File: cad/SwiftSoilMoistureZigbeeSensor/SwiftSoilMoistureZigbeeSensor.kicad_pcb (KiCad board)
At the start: 2 copper layers, 12 parts, among them J1 Probe, J2 BAT, J3 TagConnect, Q1 BSS84, SW1 Factory Reset, U1 TPS61221DCK, U2 E73-2G4M08S1C

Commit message: CAD Stuff
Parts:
- added JP1: Jumper_Prog, Connector_PinHeader_2.54mm:PinHeader_1x02_P2.54mm_Vertical, F.Cu at (119.9, 71.2)
- J3: value TagConnect -> Conn_ARM_JTAG_SWD_10; footprint Connector:Tag-Connect_TC2030-IDC-NL_2x03_P1.27mm_Vertical -> Connector_PinHeader_1.27mm:PinHeader_2x05_P1.27mm_Vertical_SMD
- moved D1 64.9 mm to (112.0, 72.5)
- moved R1 64.6 mm to (107.5, 72.5)
- moved Q1 62.3 mm to (66.9, 68.7)
- moved SW1 62.3 mm to (99.4, 71.5)
- moved U2 62.3 mm to (82.2, 66.0)
- moved J1 61.1 mm to (61.5, 71.2)
- moved J3 60.9 mm to (109.1, 62.3), turned to 180 degrees
- moved C2 56.6 mm to (124.2, 60.3)
- moved U1 56.6 mm to (127.9, 60.5)
- moved C1 56.6 mm to (131.1, 60.3)
- moved L1 56.6 mm to (129.9, 65.4)
- moved J2 53.5 mm to (140.2, 63.6), turned to 180 degrees
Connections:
- C2 pad 1: +3.3V -> Net-(JP1-A)
- J3 pad 3: Net-(J3-~{RESET}) -> GND
- Q1 pad 2: +3.3V -> Net-(JP1-A)
- U1 pad 2: +3.3V -> Net-(JP1-A)
- U1 pad 4: +3.3V -> Net-(JP1-A)
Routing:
- net GND: track 0.00 -> 125.6 mm, vias 0 -> 1
- net Net-(JP1-A): track 0.00 -> 77.7 mm
- net Net-(J3-~{RESET}): track 0.00 -> 36.7 mm
- net +3.3V: track 38.2 -> 53.1 mm
- net Net-(J2-Pin_1): track 65.3 -> 74.7 mm
- net Net-(U2B-P0.24): track 8.08 -> 16.0 mm
- net Net-(J1-Pin_1): track 18.4 -> 15.3 mm
- net Net-(U2B-P0.13): track 23.2 -> 20.8 mm
- net Net-(J1-Pin_2): track 7.62 -> 6.35 mm
- net Net-(J3-SWCLK/TCK): track 19.5 -> 18.6 mm
- net Net-(J3-SWDIO/TMS): track 17.9 -> 18.6 mm
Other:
- board outline added: 83.8 x 22.9 mm

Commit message: Prints
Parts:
- J3: value Conn_ARM_JTAG_SWD_10 -> ARM SWD 10
- JP1: value Jumper_Prog -> Prog
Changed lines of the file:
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@@
     (property "ki_keywords" "Cortex Debug Connector ARM SWD JTAG")
     (attr smd)
-    (fp_text reference "J3" (at 0 -4.235) (layer "F.SilkS")
-        (effects (font (size 1 1) (thickness 0.15)))
-    )
-    (fp_text value "Conn_ARM_JTAG_SWD_10" (at 0 4.235) (layer "F.Fab")
+    (fp_text reference "J3" (at 1.1915 -4.9635) (layer "F.SilkS")
+        (effects (font (size 1 1) (thickness 0.15)))
+    )
+    (fp_text value "ARM SWD 10" (at 0 4.235) (layer "F.Fab")
         (effects (font (size 1 1) (thickness 0.15)))
     )
@@
     (property "ki_keywords" "LED diode")
     (attr smd)
-    (fp_text reference "D1" (at 0 -1.05) (layer "F.SilkS")
-        (effects (font (size 1 1) (thickness 0.15)))
-    )
-    (fp_text value "LED" (at 0 1.05) (layer "F.Fab")
+    (fp_text reference "D1" (at -1.0785 -1.05 90) (layer "F.SilkS")
+        (effects (font (size 1 1) (thickness 0.15)))
+    )
+    (fp_text value "LED" (at -1.0785 2.6565 90) (layer "F.Fab")
         (effects (font (size 1 1) (thickness 0.15)))
     )
@@
         (effects (font (size 1 1) (thickness 0.15)))
     )
-    (fp_text value "Jumper_Prog" (at 0 4.87) (layer "F.Fab")
+    (fp_text value "Prog" (at 0 4.87) (layer "F.Fab")
         (effects (font (size 1 1) (thickness 0.15)))
     )
@@
         (effects (font (size 1 1) (thickness 0.15)))
     )
-    (fp_text value "Factory Reset" (at 0 4.5) (layer "F.Fab")
+    (fp_text value "Factory Reset" (at 0 4.6735) (layer "F.Fab")
         (effects (font (size 1 1) (thickness 0.15)))
     )
@@
     (property "ki_keywords" "R res resistor")
     (attr smd)
-    (fp_text reference "R1" (at 0 -1.05) (layer "F.SilkS")
-        (effects (font (size 1 1) (thickness 0.15)))
-    )
-    (fp_text value "220ohms" (at 0 1.05) (layer "F.Fab")
+    (fp_text reference "R1" (at 0 2.4235 90) (layer "F.SilkS")
+        (effects (font (size 1 1) (thickness 0.15)))
+    )
+    (fp_text value "220ohms" (at 1.7085 -0.1165 90) (layer "F.Fab")
         (effects (font (size 1 1) (thickness 0.15)))
     )
@@
         (effects (font (size 1 1) (thickness 0.15)))
     )
-    (fp_text value "E73-2G4M08S1C" (at 1.905 10.795) (layer "F.Fab")
-        (effects (font (size 1 1) (thickness 0.15)))
-    )
+    (fp_text value "E73-2G4M08S1C" (at 1.631 11.48) (layer "F.Fab")
+        (effects (font (size 1 1) (thickness 0.15)))
+    )

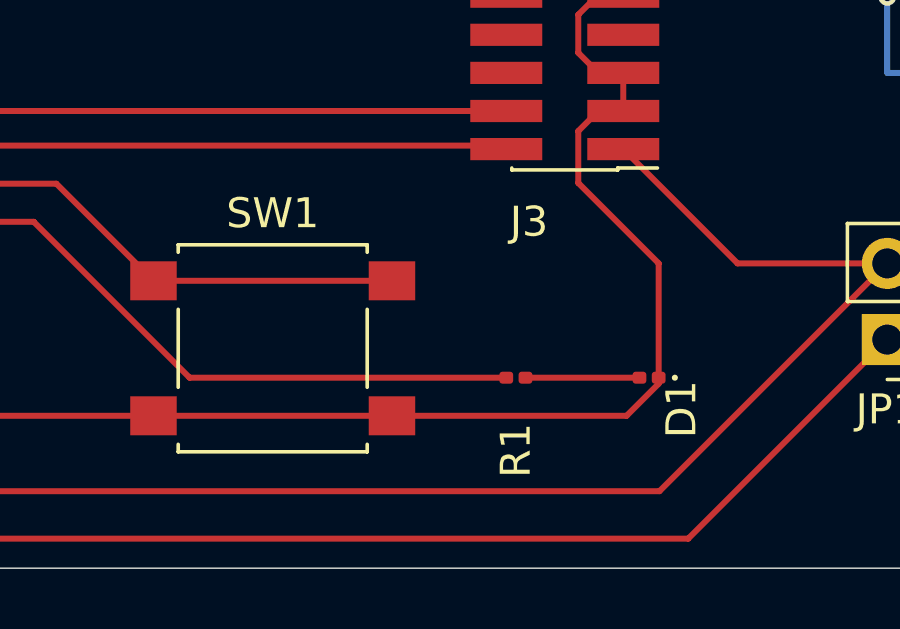
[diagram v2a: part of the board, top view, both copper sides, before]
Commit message: LED and R1 sizes to 0603
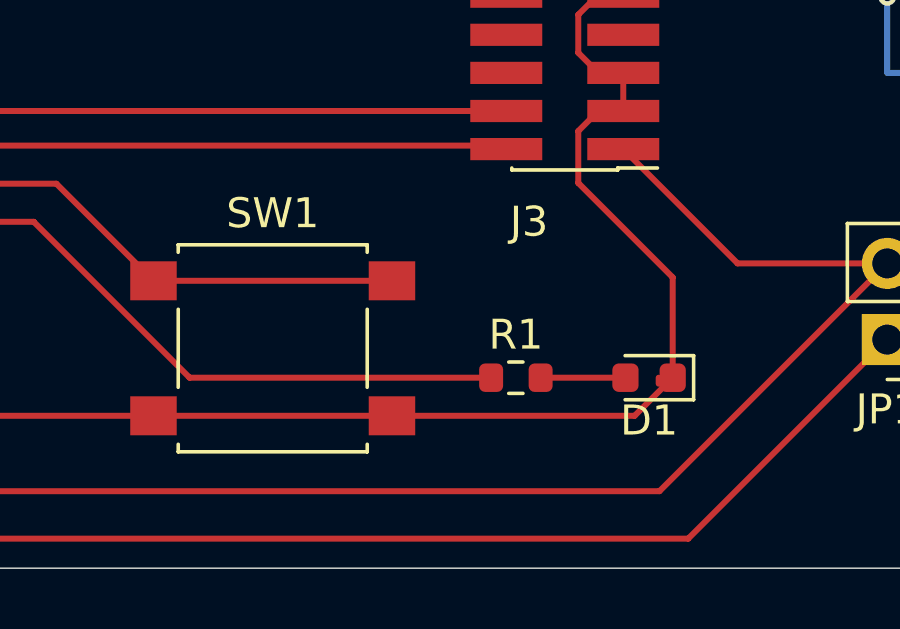
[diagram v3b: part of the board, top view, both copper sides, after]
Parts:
- D1: footprint LED_SMD:LED_0201_0603Metric -> LED_SMD:LED_0603_1608Metric
- J3: value ARM SWD 10 -> Conn_ARM_JTAG_SWD_10
- JP1: value Prog -> Jumper_Prog
- R1: footprint Resistor_SMD:R_0201_0603Metric -> Resistor_SMD:R_0603_1608Metric
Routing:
- net Net-(D1-A): track 3.80 -> 2.83 mm
- net GND: track 125.6 -> 126.4 mm
- net Net-(U2B-P0.13): track 20.8 -> 20.3 mm

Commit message: Comp Label renaming
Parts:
- J3: value Conn_ARM_JTAG_SWD_10 -> ARM SWD 10
- R1: value 220ohms -> 220Ω
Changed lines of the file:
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@@
         (effects (font (size 1 1) (thickness 0.15)))
     )
-    (fp_text value "Conn_ARM_JTAG_SWD_10" (at 0 4.235) (layer "F.Fab")
+    (fp_text value "ARM SWD 10" (at 0 4.235) (layer "F.Fab")
         (effects (font (size 1 1) (thickness 0.15)))
     )
@@
         (effects (font (size 1 1) (thickness 0.15)))
     )
-    (fp_text value "220ohms" (at 0 1.43) (layer "F.Fab")
-        (effects (font (size 1 1) (thickness 0.15)))
-    )
+    (fp_text value "220Ω" (at 0 1.43) (layer "F.Fab")
+        (effects (font (size 1 1) (thickness 0.15)))
+    )

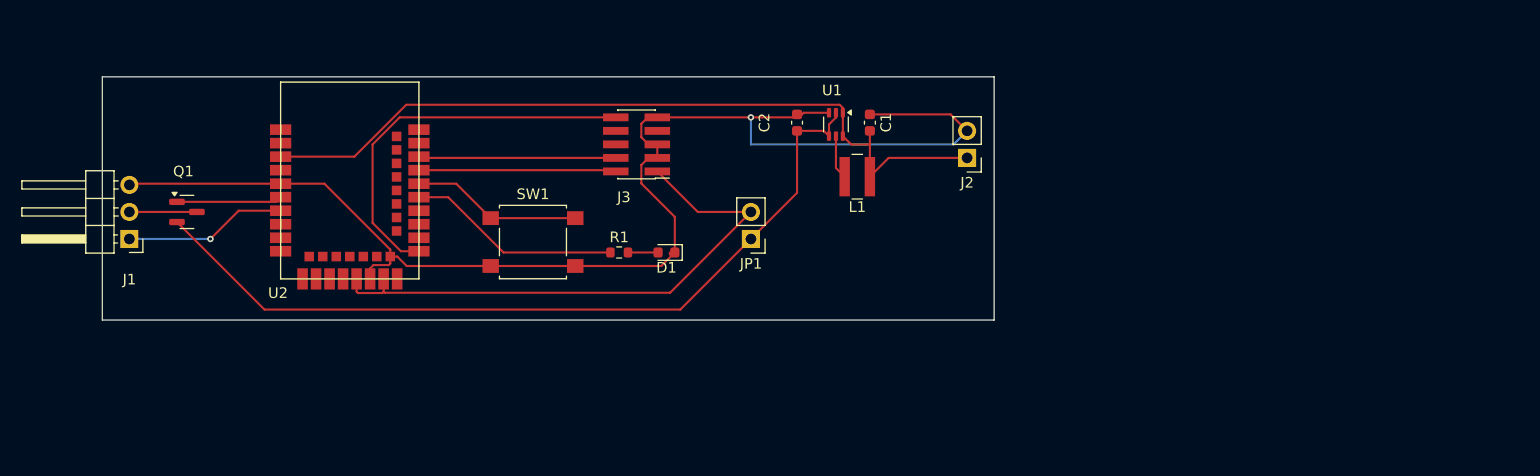
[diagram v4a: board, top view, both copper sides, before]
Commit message: Ground planes
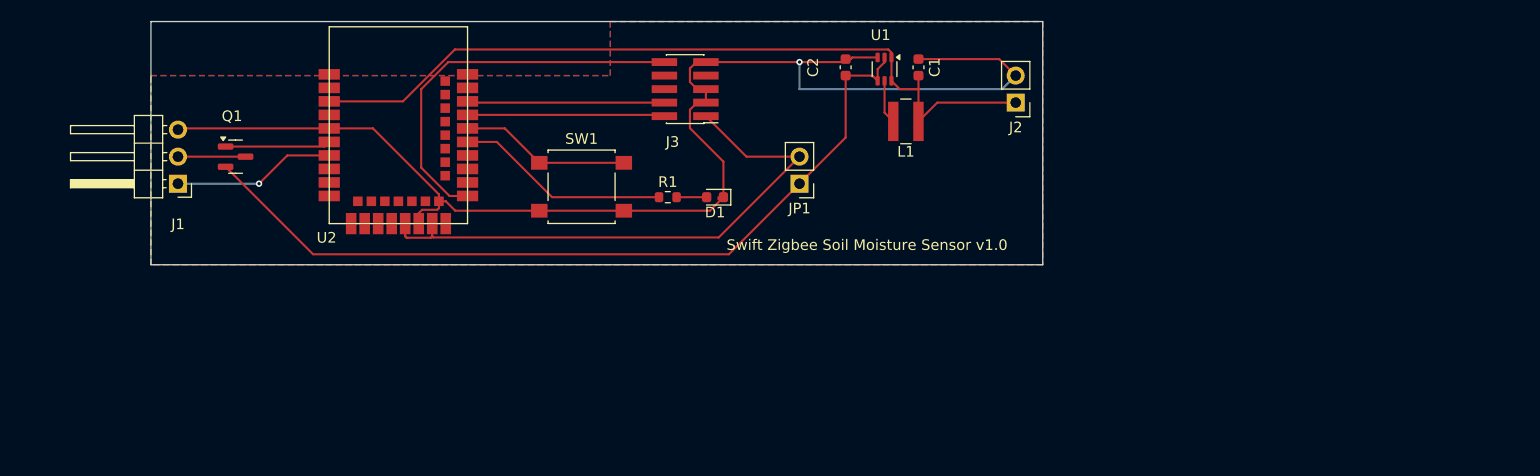
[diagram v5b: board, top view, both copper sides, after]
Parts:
- moved C2 6.92 mm to (128.8, 55.1)
- moved J1 6.92 mm to (66.0, 66.0)
- moved C1 6.92 mm to (135.6, 55.1)
- moved D1 6.92 mm to (116.5, 67.3)
- moved J2 6.92 mm to (144.8, 58.4)
- moved J3 6.92 mm to (113.7, 57.1)
- moved JP1 6.92 mm to (124.5, 66.0)
- moved L1 6.92 mm to (134.5, 60.2)
- moved Q1 6.92 mm to (71.5, 63.5)
- moved R1 6.92 mm to (112.1, 67.3)
- moved SW1 6.92 mm to (104.0, 66.3)
- moved U2 6.92 mm to (86.8, 60.8)
- moved U1 6.92 mm to (132.5, 55.3)
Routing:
- added copper zone on B.Cu, net GND
- added copper zone on F.Cu, net GND
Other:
- board text added: "Swift Zigbee Soil Moisture Sensor v1.0"
